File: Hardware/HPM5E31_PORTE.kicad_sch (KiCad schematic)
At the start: 1 part, among them U1 HPM5E31IGN1

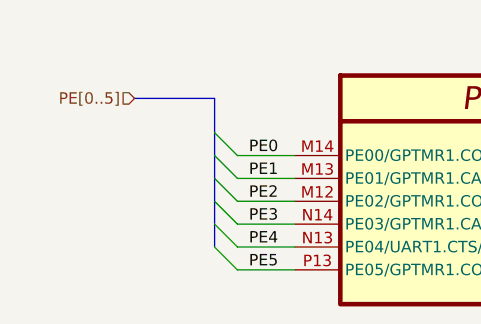
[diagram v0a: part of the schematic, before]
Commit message: 新增ESC IO引出，ESC CTR LED，EUI接口
编码器接口电源输出加保险，SPI加ESD
PY32ADC外部接口加ESD
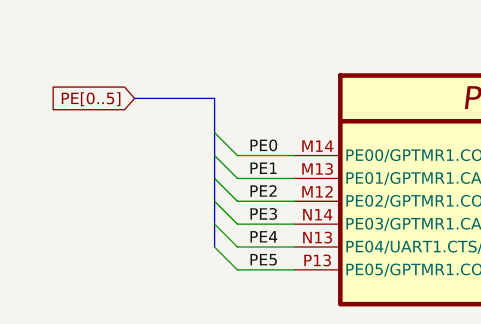
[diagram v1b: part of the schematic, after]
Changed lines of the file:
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@@
 		)
 	)
-	(hierarchical_label "PE[0..5]"
+	(global_label "PE[0..5]"
 		(shape input)
 		(at 52.07 73.66 180)
+		(fields_autoplaced yes)
 		(effects
 			(font
@@
 			(justify right)
 		)
+		(property "Intersheetrefs" "${INTERSHEET_REFS}"
+			(at 41.3438 73.66 0)
+			(effects
+				(font
+					(size 1.27 1.27)
+				)
+				(justify right)
+				(hide yes)
+			)
+		)
 	)

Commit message: 拉线
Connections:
- net PE0: now also U1.M2 (DCDC_IN); no longer U1.M14 (PE00/GPTMR1.COMP0/UART0.TXD/MCAN0.TXD/ESC0.CTR4/PPI0.CTR4/PWM0.P0/TRGM.P00/QEO1.A/USB0.ID/ETH0.EVTO1/ESC0.EVTO1)
- net PE1: no longer U1.M13 (PE01/GPTMR1.CAPT0/UART0.RXD/MCAN0.RXD/ESC0.CTR5/PPI0.CTR5/PWM0.P1/TRGM.P01/QEO1.B/USB0.PWR)
- net PE2: no longer U1.M12 (PE02/GPTMR1.COMP1/UART0.DE/UART0.RTS/I2C2.SCL/MCAN0.STBY/ESC0.CTR6/PPI0.CTR6/PWM0.P2/TRGM.P02/QEO1.Z)
- net PE3: now also U1.N2 (DCDC_LP); no longer U1.N14 (PE03/GPTMR1.CAPT1/UART0.CTS/I2C2.SDA/MCAN1.STBY/ESC0.CTR1/PPI0.CTR7/PWM0.P3/TRGM.P03/USB0.OC)
- net PE4: now also U1.P3 (DCDC_LP); no longer U1.N13 (PE04/UART1.CTS/MCAN1.RXD/ESC0.CTR2/PWM0.P4/TRGM.P04/ETH0.COL/ETH0.EVTI1/ESC0.EVTI1)
- net PE5: no longer U1.P13 (PE05/GPTMR1.COMP2/UART1.DE/UART1.RTS/MCAN1.TXD/ESC0.CTR3/PWM0.P5/TRGM.P05/ETH0.CRS)
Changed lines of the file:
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@@
 		(lib_id "HPM5E00_Library:HPM5E31IGN1")
 		(at 74.93 71.12 0)
-		(unit 8)
+		(unit 1)
 		(exclude_from_sim no)
 		(in_bom yes)
@@
 		(pin "L6"
 		)
-		(instances
-			(project "HPM5E31_ECatDualFOC"
-				(path "/a07e9810-3899-4327-ba8f-f24142a7c70e/b9a8d5a3-7d25-4818-87f6-adc719379948/2d4a5fa8-008b-4423-85d3-728409cae44f"
-					(reference "U1")
-					(unit 8)
-				)
-			)
-		)
 	)

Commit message: 修存档拉线
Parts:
- renumbered U1 to U3
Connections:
- net PE0: now also U3.M14 (PE00/GPTMR1.COMP0/UART0.TXD/MCAN0.TXD/ESC0.CTR4/PPI0.CTR4/PWM0.P0/TRGM.P00/QEO1.A/USB0.ID/ETH0.EVTO1/ESC0.EVTO1); no longer U3.M2 (DCDC_IN)
- net PE1: now also U3.M13 (PE01/GPTMR1.CAPT0/UART0.RXD/MCAN0.RXD/ESC0.CTR5/PPI0.CTR5/PWM0.P1/TRGM.P01/QEO1.B/USB0.PWR)
- net PE2: now also U3.M12 (PE02/GPTMR1.COMP1/UART0.DE/UART0.RTS/I2C2.SCL/MCAN0.STBY/ESC0.CTR6/PPI0.CTR6/PWM0.P2/TRGM.P02/QEO1.Z)
- net PE3: now also U3.N14 (PE03/GPTMR1.CAPT1/UART0.CTS/I2C2.SDA/MCAN1.STBY/ESC0.CTR1/PPI0.CTR7/PWM0.P3/TRGM.P03/USB0.OC); no longer U3.N2 (DCDC_LP)
- net PE4: now also U3.N13 (PE04/UART1.CTS/MCAN1.RXD/ESC0.CTR2/PWM0.P4/TRGM.P04/ETH0.COL/ETH0.EVTI1/ESC0.EVTI1); no longer U3.P3 (DCDC_LP)
- net PE5: now also U3.P13 (PE05/GPTMR1.COMP2/UART1.DE/UART1.RTS/MCAN1.TXD/ESC0.CTR3/PWM0.P5/TRGM.P05/ETH0.CRS)
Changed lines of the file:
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@@
 		(lib_id "HPM5E00_Library:HPM5E31IGN1")
 		(at 74.93 71.12 0)
-		(unit 1)
+		(unit 8)
 		(exclude_from_sim no)
 		(in_bom yes)
@@
 		(dnp no)
 		(fields_autoplaced yes)
-		(property "Reference" "U1"
+		(property "Reference" "U3"
 			(at 141.605 66.04 0)
 			(effects
@@
 		(pin "L6"
 		)
+		(instances
+			(project "HPM5E31_ECatDualFOC"
+				(path "/a07e9810-3899-4327-ba8f-f24142a7c70e/b9a8d5a3-7d25-4818-87f6-adc719379948/2d4a5fa8-008b-4423-85d3-728409cae44f"
+					(reference "U3")
+					(unit 8)
+				)
+			)
+		)
 	)
